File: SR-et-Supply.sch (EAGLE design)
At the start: 14 parts

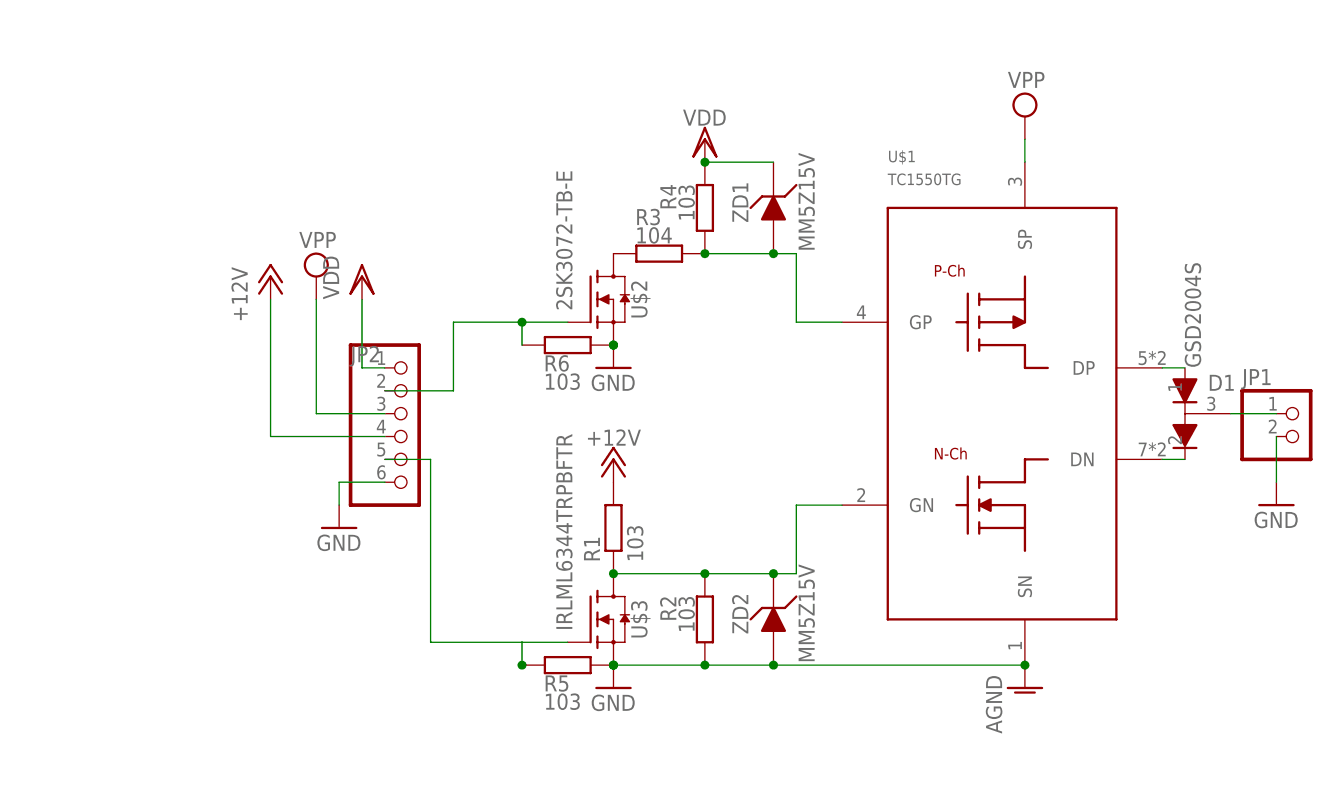
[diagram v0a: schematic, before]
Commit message: Make Source Follwer FET derived from the existing test board to SR-et-Supply, and added ShiftResistor to it
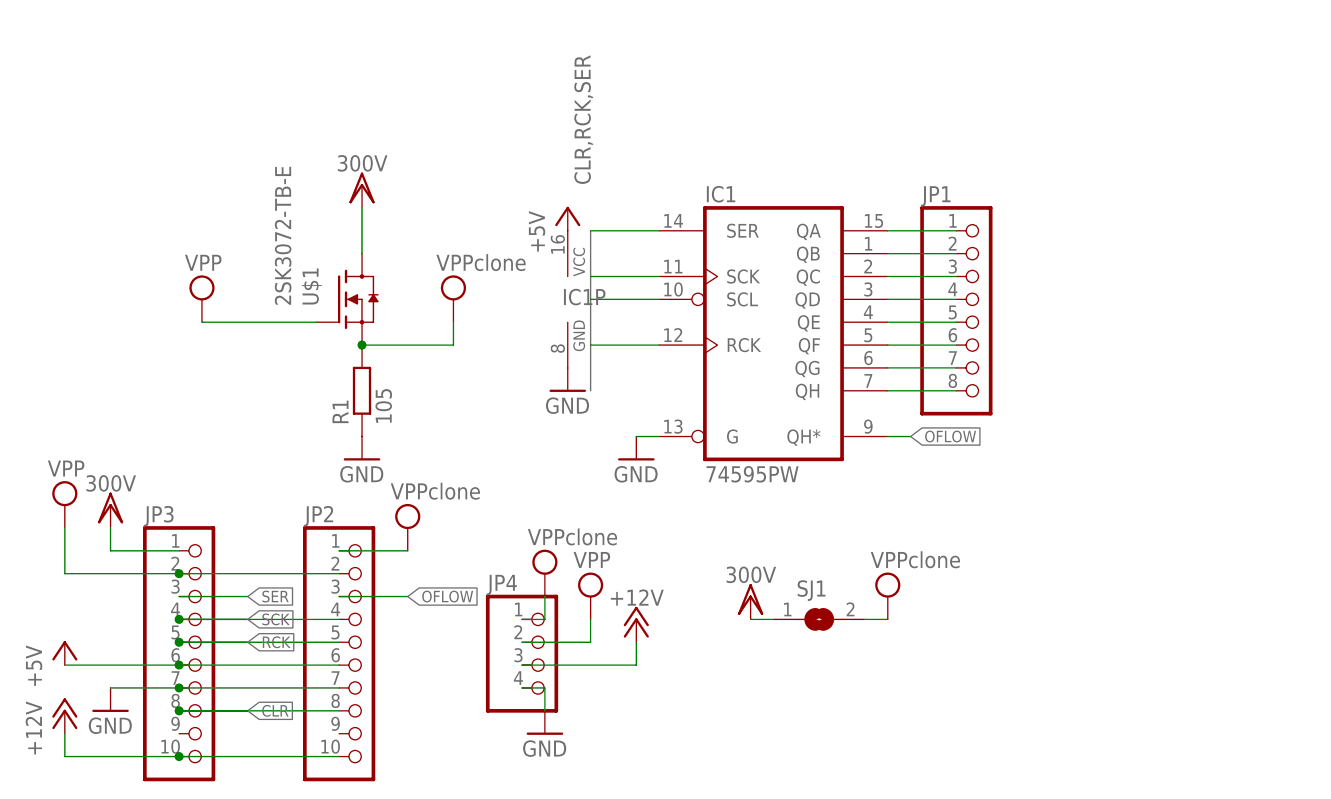
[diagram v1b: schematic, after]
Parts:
- removed D1: GSD2004S, Diode_Vishay:GSD2004S
- removed R2, R4, R5, R6: 103, rcl:R-EU_0204/5
- removed R3: 104, rcl:R-EU_0204/5
- removed U$2: 2SK3072-TB-E, Transistor-FET:2SK3072-TB-E
- removed U$3: IRLML6344TRPBFTR, Transistor-FET:IRLML6344TRPBFTR
- removed ZD1, ZD2: MM5Z15V, fairchild-semic:MM5Z15V
- added IC1: 74595PW, 74xx-eu:74595PW
- added JP3: (no value), pinhead:PINHD-1X10
- added JP4: (no value), pinhead:PINHD-1X4
- added SJ1: (no value), jumper:SJ
- JP1: device pinhead:PINHD-1X2 -> pinhead:PINHD-1X8
- JP2: device pinhead:PINHD-1X6 -> pinhead:PINHD-1X10
- R1: value 103 -> 105
- U$1: value TC1550TG -> 2SK3072-TB-E; device TC1550:TC1550TG -> Transistor-FET:2SK3072-TB-E
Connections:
- removed net VDD: JP2.1, R4.2, ZD1.K
- new net +5V: IC1P.VCC, JP2.6, JP3.6
- new net 300V: JP3.1, SJ1.1, U$1.D
- new net CLR: IC1A.SCL, JP2.8, JP3.8
- new net OFLOW: IC1A.QH*, JP2.3
- new net RCK: IC1A.RCK, JP2.5, JP3.5
- new net SCK: IC1A.SCK, JP2.4, JP3.4
- new net SER: IC1A.SER, JP3.3
- new net VPPCLONE: JP2.1, JP4.1, R1.2, SJ1.2, U$1.S
- net +12V: now also JP2.10, JP3.10, JP4.3; no longer JP2.4, R1.2
- net GND: now also IC1A.G, IC1P.GND, JP2.7, JP3.7, JP4.4, R1.1; no longer JP1.2, JP2.6, R2.1, R5.1, R6.1, U$1.SN, U$2.S, U$3.S, ZD2.P$1
- net N$1: now also IC1A.QA, JP1.1; no longer R1.1, R2.2, U$1.GN, U$3.D, ZD2.K
- net N$2: now also IC1A.QB, JP1.2; no longer R3.1, U$2.D
- net N$3: now also IC1A.QC, JP1.3; no longer R3.2, R4.1, U$1.GP, ZD1.P$1
- net N$4: now also IC1A.QD, JP1.4; no longer JP2.5, R5.2, U$3.G
- net N$5: now also IC1A.QE, JP1.5; no longer JP2.2, R6.2, U$2.G
- net N$7: now also IC1A.QF, JP1.6; no longer D1.P$1, U$1.DP
- net N$8: now also IC1A.QG, JP1.7; no longer D1.P$2, U$1.DN
- net N$9: now also IC1A.QH, JP1.8; no longer D1.P$3, JP1.1
- net VPP: now also JP2.2, JP3.2, JP4.2, U$1.G; no longer JP2.3, U$1.SP
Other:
- moved on the sheet: R1
